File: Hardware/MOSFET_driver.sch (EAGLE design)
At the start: 11 parts, among them Q1 FDS6630A

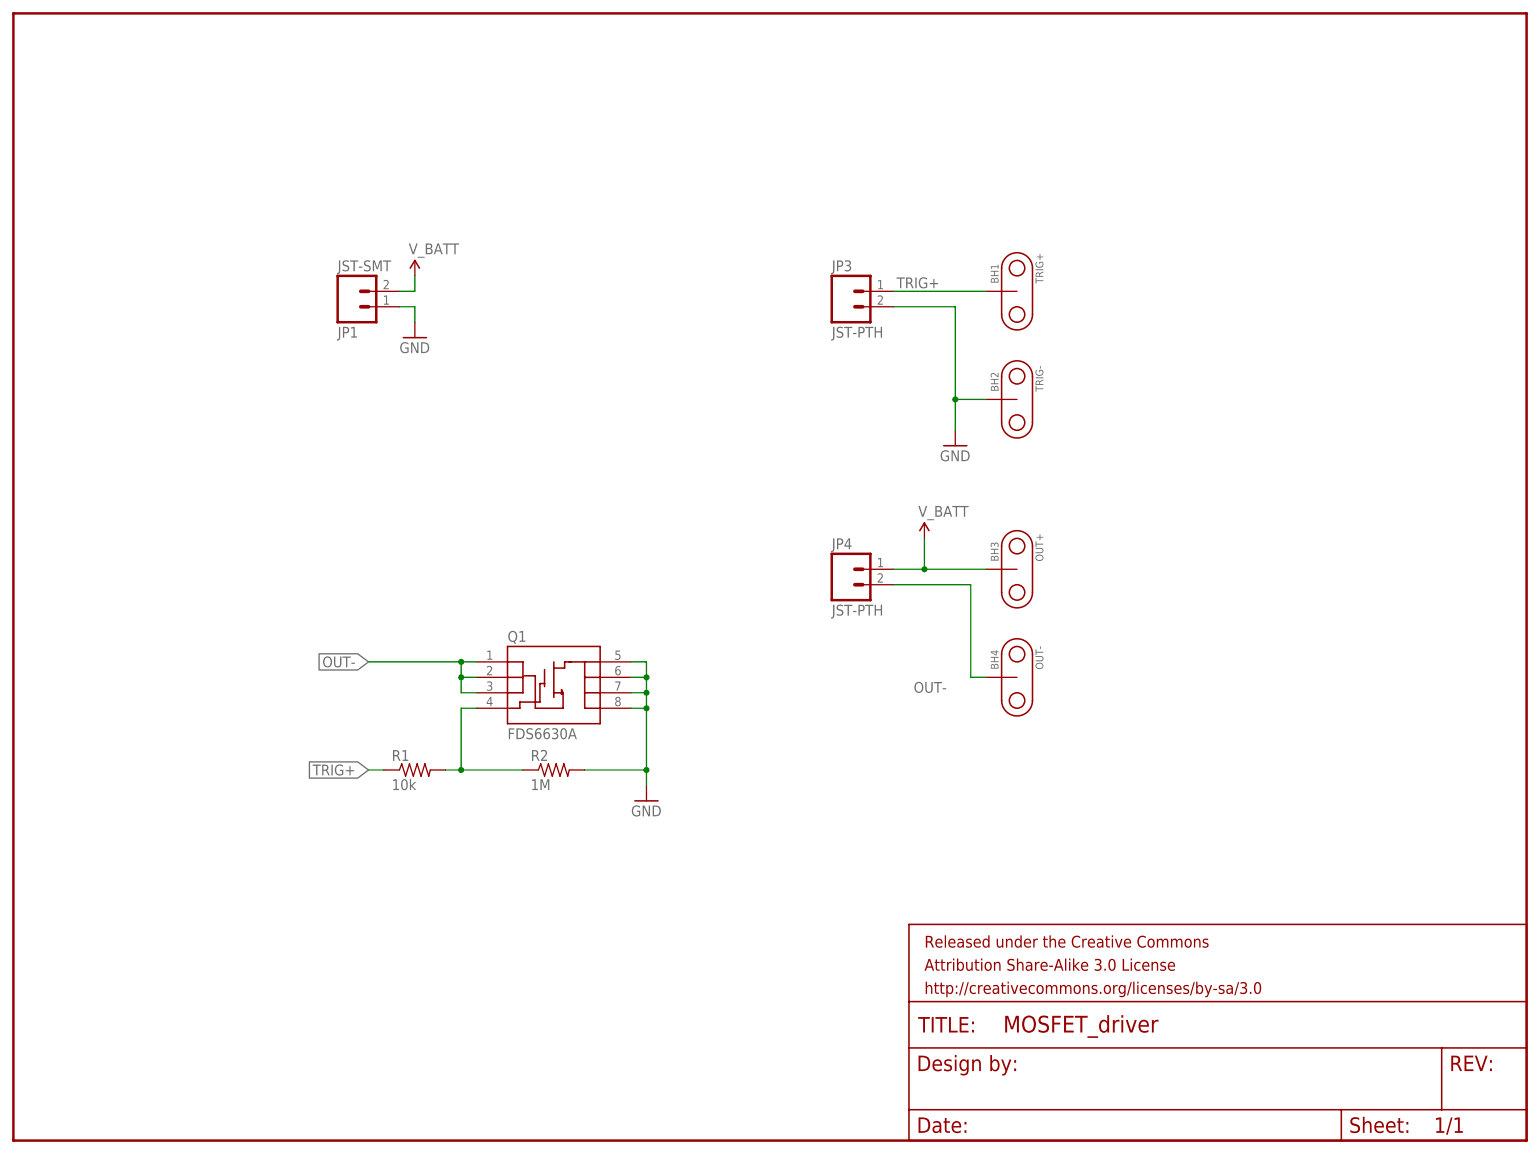
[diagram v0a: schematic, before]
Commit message: Swap source and drain pins.
The original schematic symbol isn't clear on which pins are drain
and which are source, so I screwed it up. The MOSFET was always
conducting through the body diode.

This version fixes it and should be considered for release.
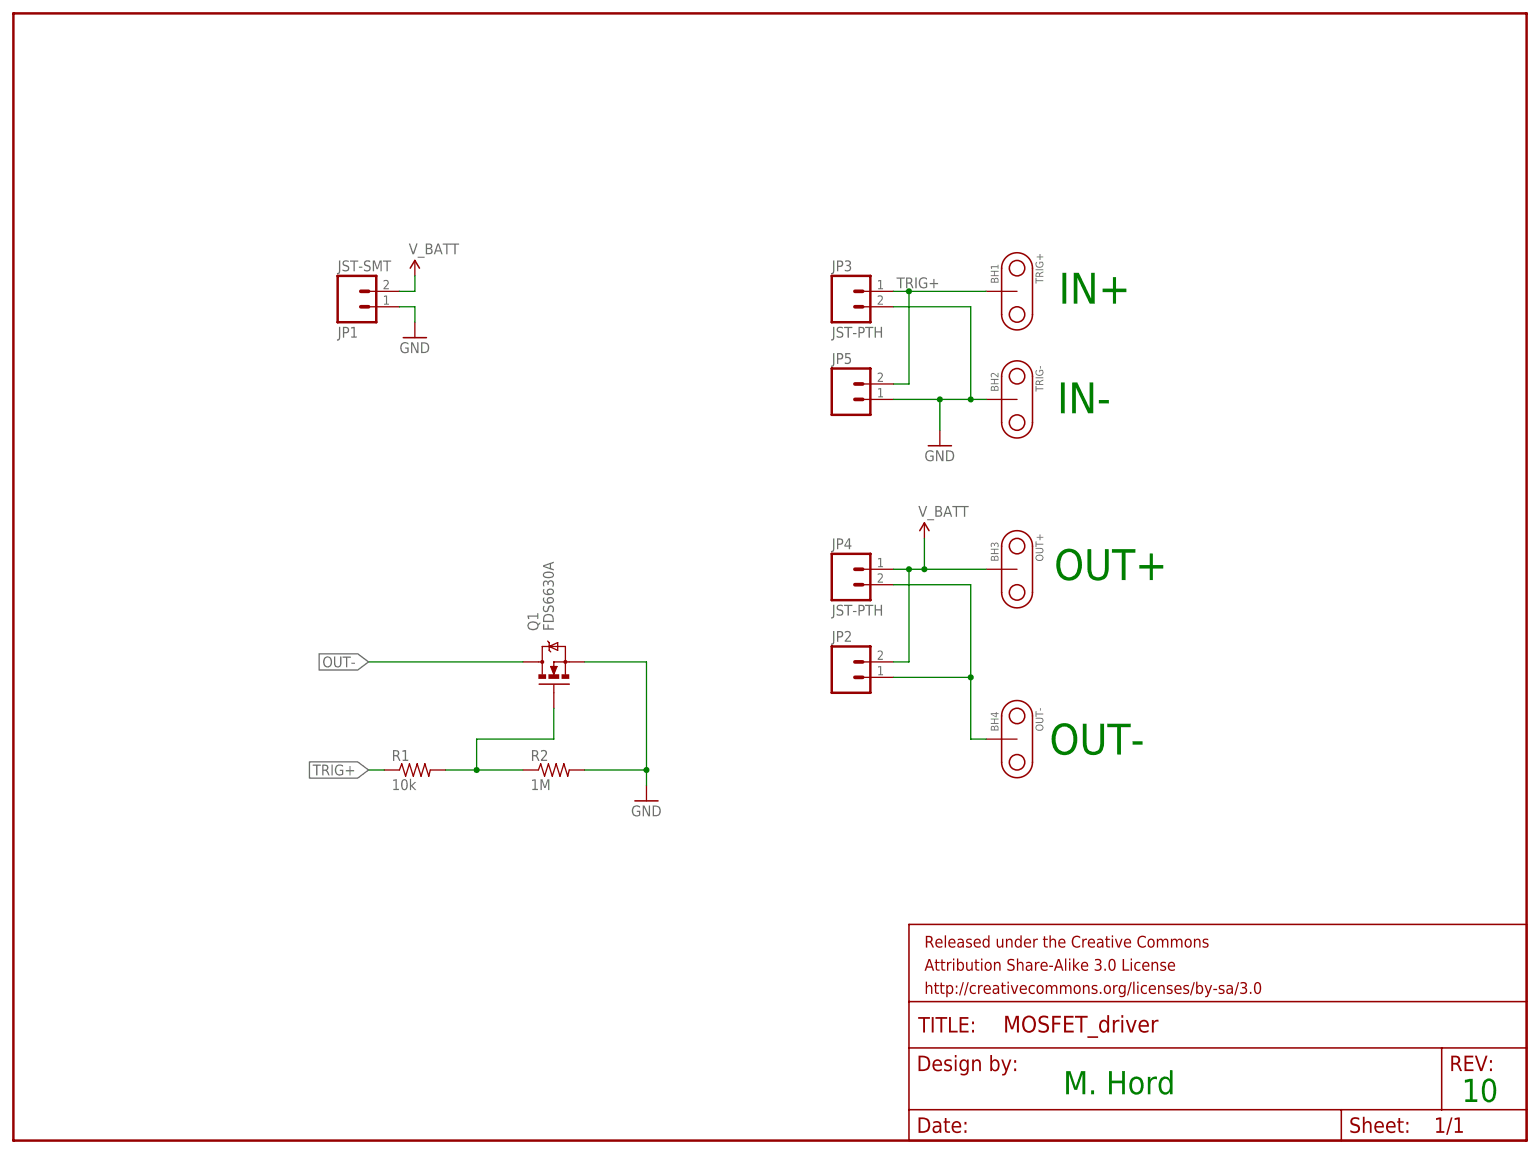
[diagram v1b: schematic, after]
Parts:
- added JP2, JP5: (no value), SparkFun-Connectors:M02PTH
- Q1: device SparkFun-DiscreteSemi:MOSFET-NCHANNEL-SOIC8 -> SparkFun-DiscreteSemi:MOSFET-NCHANNELFDS6630A; PROD_ID IC-08089 -> (none)
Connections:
- net GND: now also JP5.1, Q1.S; no longer Q1.D@1, Q1.D@2, Q1.D@3, Q1.D@4
- net OUT-: now also JP2.1, Q1.D; no longer Q1.S@1, Q1.S@2, Q1.S@3
- net TRIG+: now also JP5.2
- net V_BATT: now also JP2.2
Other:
- note added: "10"
- note added: "IN+"
- note added: "IN-"
- note added: "M. Hord"
- note added: "OUT+"
- note added: "OUT-"
- moved on the sheet: BH4

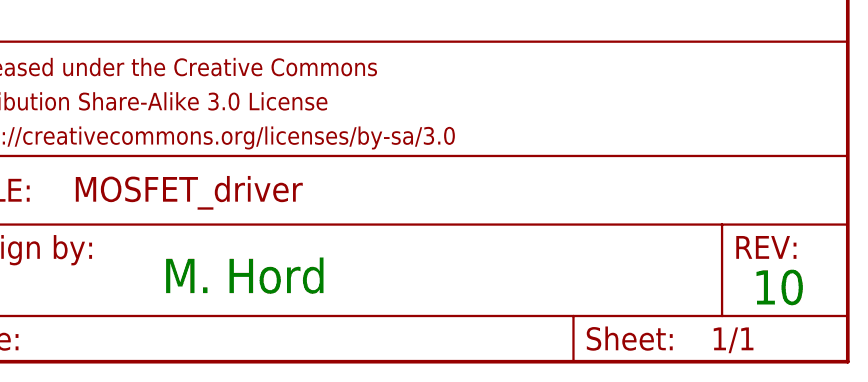
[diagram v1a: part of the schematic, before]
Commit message: RedBoard release v10 Rotate MOSFET 180 degrees. Fixed flame on silk overlapping MOSFET. Added .1" headers at either end.
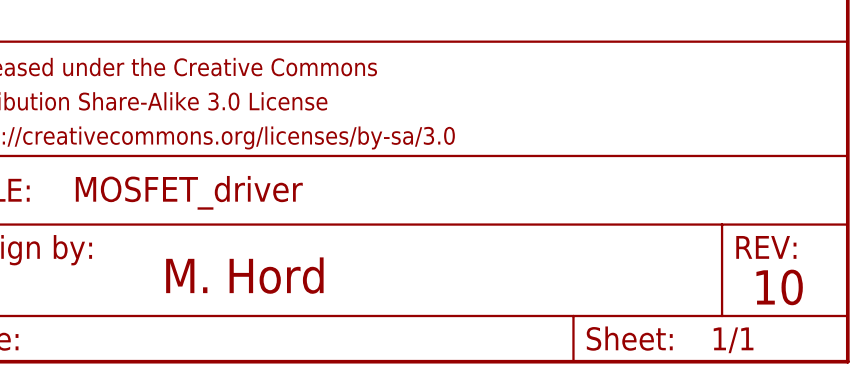
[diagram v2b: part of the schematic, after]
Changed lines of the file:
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@@
 <sheet>
 <plain>
-<text x="172.72" y="7.62" size="3.81" layer="91">M. Hord</text>
-<text x="238.252" y="6.35" size="3.81" layer="91">10</text>
+<text x="172.72" y="7.62" size="3.81" layer="94">M. Hord</text>
+<text x="238.252" y="6.35" size="3.81" layer="94">10</text>
 <text x="171.958" y="137.668" size="5.08" layer="91">IN+</text>
 <text x="171.704" y="119.634" size="5.08" layer="91">IN-</text>

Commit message: Production readied
added fiducial reference points and created panel for manufacture
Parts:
- added JP6, JP7: FIDUCIALUFIDUCIAL, SparkFun:FIDUCIALUFIDUCIAL
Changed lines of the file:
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@@
 <part name="JP2" library="SparkFun-Connectors" deviceset="M02" device="PTH"/>
 <part name="JP5" library="SparkFun-Connectors" deviceset="M02" device="PTH"/>
+<part name="JP6" library="SparkFun" deviceset="FIDUCIAL" device="UFIDUCIAL"/>
+<part name="JP7" library="SparkFun" deviceset="FIDUCIAL" device="UFIDUCIAL"/>
 </parts>
 <sheets>
@@
 <instance part="JP2" gate="G$1" x="137.16" y="76.2"/>
 <instance part="JP5" gate="G$1" x="137.16" y="121.92"/>
+<instance part="JP6" gate="G$1" x="243.84" y="33.02"/>
+<instance part="JP7" gate="G$1" x="243.84" y="27.94"/>
 </instances>
 <busses>
